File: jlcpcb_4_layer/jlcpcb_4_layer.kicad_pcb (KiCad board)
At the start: 4 copper layers, 2 parts

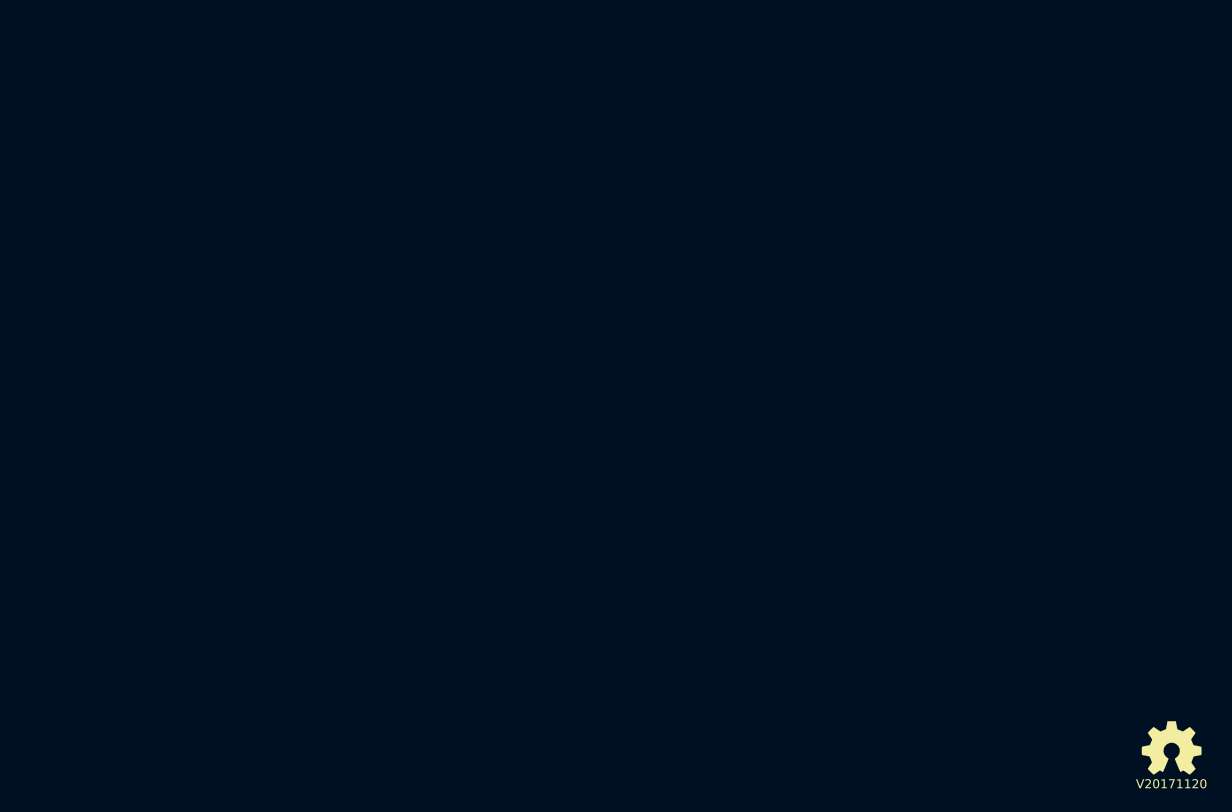
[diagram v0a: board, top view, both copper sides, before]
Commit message: updated jlcpcb 4 layer template to kicad6
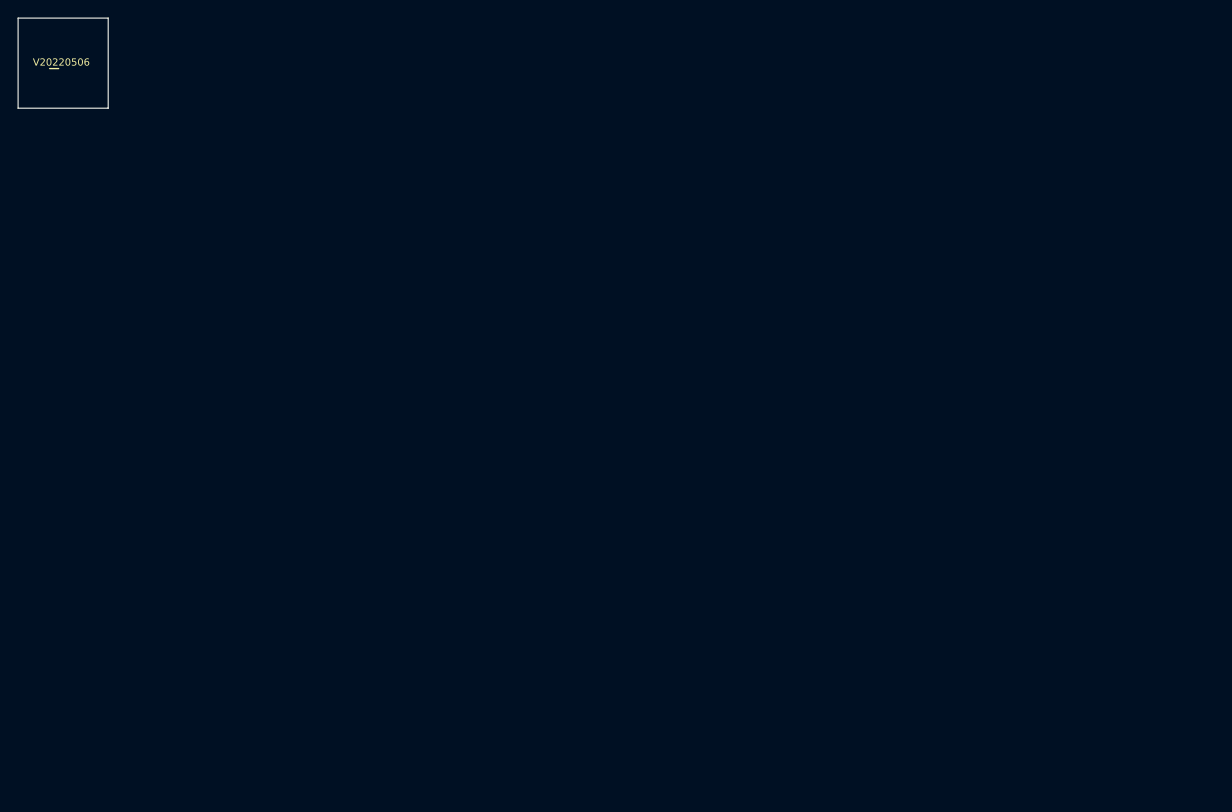
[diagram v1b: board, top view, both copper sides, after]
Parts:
- removed N2: V20171120, SquantorLabels:Label_version
- N1: value OHWLOGO -> V20220506; footprint Symbols:OSHW-Symbol_6.7x6mm_SilkScreen -> SquantorLabels:Label_Generic
- moved N1 145.4 mm to (24.0, 25.0)
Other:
- board outline added: 10 x 10 mm
- net class Default removed
- rule pad_to_mask_clearance: 0.2 -> 0.05
